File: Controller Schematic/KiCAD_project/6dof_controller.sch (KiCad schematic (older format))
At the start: 111 parts, among them J1 Screw_Terminal_01x03, J10 Conn_02x13_Top_Bottom, J2 DS-201, J3 RJ45, J4 Conn_02x13_Top_Bottom, J5 Conn_02x13_Top_Bottom, J6 Conn_02x13_Top_Bottom, J7 Conn_02x05_Top_Bottom, J8 Conn_02x13_Top_Bottom, J9 Conn_02x13_Top_Bottom, U1 4N35, U1 ESP32_DevKit_V1_DOIT, U10 4N35, U11 4N35, U12 4N35, U13 4N35, U14 4N35, U2 MCP23SigIn1M17_SP, U3 4N35, U4 4N35, U5 4N35, U6 4N35, U7 4N35, U8 4N35, U9 4N35

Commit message: I've renamed folders
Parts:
- J2: footprint Connector_BarrelJack:BarrelJack_Horizontal -> Connector_BarrelJack:BarrelJack_CUI_PJ-063AH_Horizontal
- renumbered *D11 to *D10, *D12 to *D11, *D3 to *D2, *D4 to *D3, *D5 to *D4, *D6 to *D5, *D7 to *D6, *D8 to *D7, *D9 to *D8, *D10 to *D9, *R2 to *R1, *R11 to *R10, *R12 to *R11, *R13 to *R12, *R14 to *R13, *R15 to *R14, *R16 to *R15, *R3 to *R2, *R4 to *R3, *R5 to *R4, *R6 to *R5, *R7 to *R6, *R8 to *R7, *R9 to *R8, *R10 to *R9, *U2 to *U1, *U3 to *U2, *U4 to *U3, *U5 to *U4, *U6 to *U5, *U7 to *U6, *U8 to *U7, *U9 to *U8, D2 to D1, D1 to D2, D2 to D3, D3 to D4, D4 to D5, D5 to D6, R9 to R10, R10 to R11, R11 to R12, R12 to R13, R13 to R14, R14 to R15, R1 to R2, R2 to R3, R3 to R4, R4 to R5, R5 to R6, R6 to R7, R7 to R8, R8 to R9, U9 to U10, U10 to U11, U11 to U12, U12 to U13, U13 to U14, U14 to U15, U1 to U2, U2 to U3, U3 to U4, U4 to U5, U5 to U6, U6 to U7, U7 to U8, U8 to U9

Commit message: project updated
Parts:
- removed J2: DS-201, Connector_BarrelJack:BarrelJack_CUI_PJ-063AH_Horizontal, symbol Connector:Barrel_Jack_Switch_Pin3Ring
- added J2: DS-201, Connector_BarrelJack:BarrelJack_CUI_PJ-063AH_Horizontal, symbol Connector:Barrel_Jack
- added JP4: SolderJumper_2_Open, Jumper:SolderJumper-2_P1.3mm_Open_Pad1.0x1.5mm, symbol Jumper:SolderJumper_2_Open
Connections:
- net COM: now also J2.2
- net NotSigOut1IN: now also JP4.2 (B)
- net at U3.27 (GPA6): now also JP4.1 (A)
- net at *J2.1 (Pin_1), D2.2 (A): now also J2.1
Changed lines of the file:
@@
 Wire Wire Line
 	1200 10650 1200 10250
-$Comp
-L Connector:Barrel_Jack_Switch_Pin3Ring J2
-U 1 1 601FD643
-P 900 10750
-F 0 "J2" H 950 11050 50  0000 C CNN
-F 1 "DS-201" H 957 10976 50  0000 C CNN
-F 2 "Connector_BarrelJack:BarrelJack_CUI_PJ-063AH_Horizontal" H 950 10710 50  0001 C CNN
-F 3 "https://www.chipdip.ru/product/ds-201" H 950 10710 50  0001 C CNN
-	1    900  10750
-	1    0    0    -1
-$EndComp
 Text GLabel 2500 10150 1    50   Input ~ 0
 DC12
@@
 Wire Wire Line
 	11200 4100 11300 4100
-Wire Wire Line
-	1200 10750 1200 10850
-Connection ~ 1200 10850
 Wire Bus Line
 	7500 650  7500 2050
@@
 	2550 10900 3050 10900
 Connection ~ 2550 10700
-$Comp
-L Jumper:SolderJumper_2_Open JP2
-U 1 1 602EB81E
-P 7100 2500
-F 0 "JP2" H 7250 2550 50  0000 C CNN
-F 1 "SolderJumper_2_Open" H 7100 2614 50  0001 C CNN
-F 2 "Jumper:SolderJumper-2_P1.3mm_Open_Pad1.0x1.5mm" H 7100 2500 50  0001 C CNN
-F 3 "~" H 7100 2500 50  0001 C CNN
-	1    7100 2500
-	1    0    0    -1
-$EndComp
-$Comp
-L Jumper:SolderJumper_2_Open JP3
-U 1 1 602ED0FE
-P 7100 2600
-F 0 "JP3" H 7100 2500 50  0000 C CNN
-F 1 "SolderJumper_2_Open" H 7100 2714 50  0001 C CNN
-F 2 "Jumper:SolderJumper-2_P1.3mm_Open_Pad1.0x1.5mm" H 7100 2600 50  0001 C CNN
-F 3 "~" H 7100 2600 50  0001 C CNN
-	1    7100 2600
-	1    0    0    -1
-$EndComp
 Text GLabel 7250 2500 2    50   Input ~ 0
 PanelLED
@@
 Wire Bus Line
 	7250 650  7250 5050
+$Comp
+L Jumper:SolderJumper_2_Open JP4
+U 1 1 5FCE05BC
+P 7100 2700
+F 0 "JP4" H 7250 2750 50  0000 C CNN
+F 1 "SolderJumper_2_Open" H 7100 2814 50  0001 C CNN
+F 2 "Jumper:SolderJumper-2_P1.3mm_Open_Pad1.0x1.5mm" H 7100 2700 50  0001 C CNN
+F 3 "~" H 7100 2700 50  0001 C CNN
+	1    7100 2700
+	1    0    0    -1
+$EndComp
+Text GLabel 7250 2700 2    50   Input ~ 0
+NotSigOut1IN
+$Comp
+L Jumper:SolderJumper_2_Open JP3
+U 1 1 602ED0FE
+P 7100 2600
+F 0 "JP3" H 7250 2650 50  0000 C CNN
+F 1 "SolderJumper_2_Open" H 7100 2714 50  0001 C CNN
+F 2 "Jumper:SolderJumper-2_P1.3mm_Open_Pad1.0x1.5mm" H 7100 2600 50  0001 C CNN
+F 3 "~" H 7100 2600 50  0001 C CNN
+	1    7100 2600
+	1    0    0    -1
+$EndComp
+$Comp
+L Jumper:SolderJumper_2_Open JP2
+U 1 1 602EB81E
+P 7100 2500
+F 0 "JP2" H 7250 2550 50  0000 C CNN
+F 1 "SolderJumper_2_Open" H 7100 2614 50  0001 C CNN
+F 2 "Jumper:SolderJumper-2_P1.3mm_Open_Pad1.0x1.5mm" H 7100 2500 50  0001 C CNN
+F 3 "~" H 7100 2500 50  0001 C CNN
+	1    7100 2500
+	1    0    0    -1
+$EndComp
+$Comp
+L Connector:Barrel_Jack J2
+U 1 1 5FCE9EE6
+P 900 10750
+F 0 "J2" H 957 11075 50  0000 C CNN
+F 1 "DS-201" H 957 10984 50  0000 C CNN
+F 2 "Connector_BarrelJack:BarrelJack_CUI_PJ-063AH_Horizontal" H 950 10710 50  0001 C CNN
+F 3 "https://www.chipdip.ru/product/ds-201" H 950 10710 50  0001 C CNN
+	1    900  10750
+	1    0    0    -1
+$EndComp
 $EndSCHEMATC

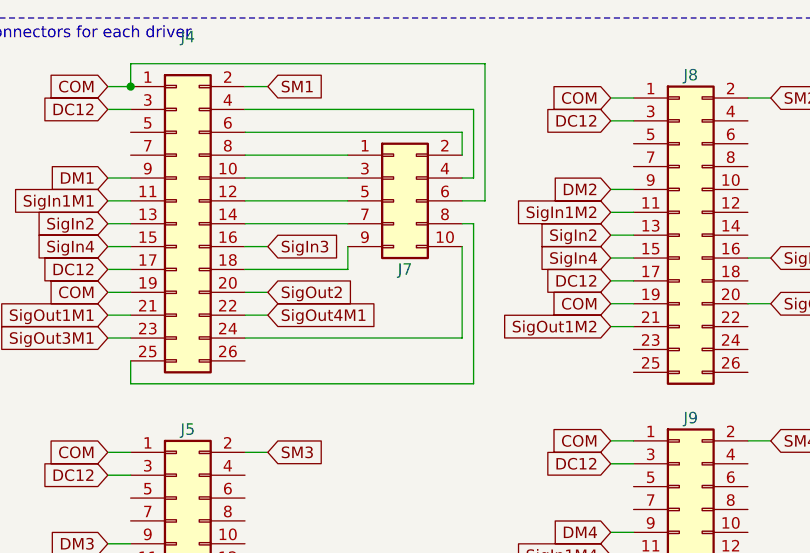
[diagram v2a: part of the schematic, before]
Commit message: I've added illustation for technical
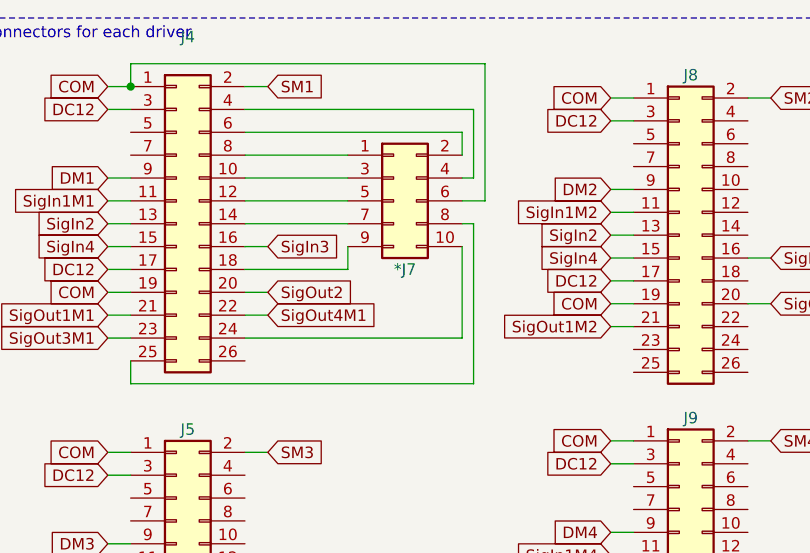
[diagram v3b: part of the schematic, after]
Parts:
- renumbered J7 to *J7
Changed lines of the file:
@@
 F 1 "1N4003" H 1500 10024 50  0000 C CNN
 F 2 "Diode_THT:D_DO-41_SOD81_P10.16mm_Horizontal" H 1500 9975 50  0001 C CNN
-F 3 "http://www.vishay.com/docs/88503/1n4001.pdf" H 1500 10150 50  0001 C CNN
+F 3 "https://www.chipdip.ru/product/1n4003-3" H 1500 10150 50  0001 C CNN
 	1    1500 10150
 	-1   0    0    1
@@
 F 1 "Conn_02x13_Top_Bottom" H 12750 3776 50  0001 C CNN
 F 2 "Connector_IDC:IDC-Header_2x13-1MP_P2.54mm_Latch_Vertical" H 12700 3050 50  0001 C CNN
-F 3 "~" H 12700 3050 50  0001 C CNN
+F 3 "https://www.chipdip.ru/product/idc-26ms" H 12700 3050 50  0001 C CNN
 	1    12700 3050
 	1    0    0    -1
@@
 F 1 "Conn_02x13_Top_Bottom" H 14950 5226 50  0001 C CNN
 F 2 "Connector_IDC:IDC-Header_2x13-1MP_P2.54mm_Latch_Vertical" H 14900 4500 50  0001 C CNN
-F 3 "~" H 14900 4500 50  0001 C CNN
+F 3 "https://www.chipdip.ru/product/idc-26ms" H 14900 4500 50  0001 C CNN
 	1    14900 4500
 	1    0    0    -1
@@
 F 1 "Conn_02x13_Top_Bottom" H 12750 5276 50  0001 C CNN
 F 2 "Connector_IDC:IDC-Header_2x13-1MP_P2.54mm_Latch_Vertical" H 12700 4550 50  0001 C CNN
-F 3 "~" H 12700 4550 50  0001 C CNN
+F 3 "https://www.chipdip.ru/product/idc-26ms" H 12700 4550 50  0001 C CNN
 	1    12700 4550
 	1    0    0    -1
@@
 F 1 "Conn_02x13_Top_Bottom" H 14950 3726 50  0001 C CNN
 F 2 "Connector_IDC:IDC-Header_2x13-1MP_P2.54mm_Latch_Vertical" H 14900 3000 50  0001 C CNN
-F 3 "~" H 14900 3000 50  0001 C CNN
+F 3 "https://www.chipdip.ru/product/idc-26ms" H 14900 3000 50  0001 C CNN
 	1    14900 3000
 	1    0    0    -1
@@
 F 1 "Conn_02x13_Top_Bottom" H 14950 2226 50  0001 C CNN
 F 2 "Connector_IDC:IDC-Header_2x13-1MP_P2.54mm_Latch_Vertical" H 14900 1500 50  0001 C CNN
-F 3 "~" H 14900 1500 50  0001 C CNN
+F 3 "https://www.chipdip.ru/product/idc-26ms" H 14900 1500 50  0001 C CNN
 	1    14900 1500
 	1    0    0    -1
@@
 	13450 1550 13450 1650
 $Comp
-L Connector_Generic:Conn_02x05_Odd_Even J7
+L Connector_Generic:Conn_02x05_Odd_Even *J7
 U 1 1 608ED766
 P 13650 1350
-F 0 "J7" H 13700 1050 50  0000 C CNN
+F 0 "*J7" H 13700 1050 50  0000 C CNN
 F 1 "Conn_02x05_Top_Bottom" H 13700 1676 50  0001 C CNN
 F 2 "Connector_IDC:IDC-Header_2x05_P2.54mm_Vertical" H 13650 1350 50  0001 C CNN
@@
 F 1 "Conn_02x13_Top_Bottom" H 12750 2176 50  0001 C CNN
 F 2 "Connector_IDC:IDC-Header_2x13-1MP_P2.54mm_Latch_Vertical" H 12700 1450 50  0001 C CNN
-F 3 "~" H 12700 1450 50  0001 C CNN
+F 3 "https://www.chipdip.ru/product/idc-26ms" H 12700 1450 50  0001 C CNN
 	1    12700 1450
 	1    0    0    -1
@@
 Text GLabel 7250 2600 2    50   Input ~ 0
 PanelIN
+$Comp
+L Jumper:SolderJumper_2_Open JP4
+U 1 1 5FCE05BC
+P 7100 2700
+F 0 "JP4" H 7250 2750 50  0000 C CNN
+F 1 "SolderJumper_2_Open" H 7100 2814 50  0001 C CNN
+F 2 "Jumper:SolderJumper-2_P1.3mm_Open_Pad1.0x1.5mm" H 7100 2700 50  0001 C CNN
+F 3 "~" H 7100 2700 50  0001 C CNN
+	1    7100 2700
+	1    0    0    -1
+$EndComp
+Text GLabel 7250 2700 2    50   Input ~ 0
+NotSigOut1IN
+$Comp
+L Jumper:SolderJumper_2_Open JP3
+U 1 1 602ED0FE
+P 7100 2600
+F 0 "JP3" H 7250 2650 50  0000 C CNN
+F 1 "SolderJumper_2_Open" H 7100 2714 50  0001 C CNN
+F 2 "Jumper:SolderJumper-2_P1.3mm_Open_Pad1.0x1.5mm" H 7100 2600 50  0001 C CNN
+F 3 "~" H 7100 2600 50  0001 C CNN
+	1    7100 2600
+	1    0    0    -1
+$EndComp
+$Comp
+L Jumper:SolderJumper_2_Open JP2
+U 1 1 602EB81E
+P 7100 2500
+F 0 "JP2" H 7250 2550 50  0000 C CNN
+F 1 "SolderJumper_2_Open" H 7100 2614 50  0001 C CNN
+F 2 "Jumper:SolderJumper-2_P1.3mm_Open_Pad1.0x1.5mm" H 7100 2500 50  0001 C CNN
+F 3 "~" H 7100 2500 50  0001 C CNN
+	1    7100 2500
+	1    0    0    -1
+$EndComp
+$Comp
+L Connector:Barrel_Jack J2
+U 1 1 5FCE9EE6
+P 900 10750
+F 0 "J2" H 957 11075 50  0000 C CNN
+F 1 "DS-201" H 957 10984 50  0000 C CNN
+F 2 "Connector_BarrelJack:BarrelJack_CUI_PJ-063AH_Horizontal" H 950 10710 50  0001 C CNN
+F 3 "https://www.chipdip.ru/product/ds-201" H 950 10710 50  0001 C CNN
+	1    900  10750
+	1    0    0    -1
+$EndComp
 Wire Bus Line
 	7800 1100 7800 2050
@@
 Wire Bus Line
 	7250 650  7250 5050
-$Comp
-L Jumper:SolderJumper_2_Open JP4
-U 1 1 5FCE05BC
-P 7100 2700
-F 0 "JP4" H 7250 2750 50  0000 C CNN
-F 1 "SolderJumper_2_Open" H 7100 2814 50  0001 C CNN
-F 2 "Jumper:SolderJumper-2_P1.3mm_Open_Pad1.0x1.5mm" H 7100 2700 50  0001 C CNN
-F 3 "~" H 7100 2700 50  0001 C CNN
-	1    7100 2700
-	1    0    0    -1
-$EndComp
-Text GLabel 7250 2700 2    50   Input ~ 0
-NotSigOut1IN
-$Comp
-L Jumper:SolderJumper_2_Open JP3
-U 1 1 602ED0FE
-P 7100 2600
-F 0 "JP3" H 7250 2650 50  0000 C CNN
-F 1 "SolderJumper_2_Open" H 7100 2714 50  0001 C CNN
-F 2 "Jumper:SolderJumper-2_P1.3mm_Open_Pad1.0x1.5mm" H 7100 2600 50  0001 C CNN
-F 3 "~" H 7100 2600 50  0001 C CNN
-	1    7100 2600
-	1    0    0    -1
-$EndComp
-$Comp
-L Jumper:SolderJumper_2_Open JP2
-U 1 1 602EB81E
-P 7100 2500
-F 0 "JP2" H 7250 2550 50  0000 C CNN
-F 1 "SolderJumper_2_Open" H 7100 2614 50  0001 C CNN
-F 2 "Jumper:SolderJumper-2_P1.3mm_Open_Pad1.0x1.5mm" H 7100 2500 50  0001 C CNN
-F 3 "~" H 7100 2500 50  0001 C CNN
-	1    7100 2500
-	1    0    0    -1
-$EndComp
-$Comp
-L Connector:Barrel_Jack J2
-U 1 1 5FCE9EE6
-P 900 10750
-F 0 "J2" H 957 11075 50  0000 C CNN
-F 1 "DS-201" H 957 10984 50  0000 C CNN
-F 2 "Connector_BarrelJack:BarrelJack_CUI_PJ-063AH_Horizontal" H 950 10710 50  0001 C CNN
-F 3 "https://www.chipdip.ru/product/ds-201" H 950 10710 50  0001 C CNN
-	1    900  10750
-	1    0    0    -1
-$EndComp
 $EndSCHEMATC

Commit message: The circuit and board were redesigned after prototyping. Removed all unnecessary. Reduced the PCB.
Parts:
- removed *D10, *D3, *D8, *D9, D1: BL-LS0805UYC, LED_SMD:LED_0805_2012Metric, symbol Device:LED
- removed *D5, *D6, *D7: BAV23, Package_TO_SOT_SMD:SOT-23, symbol Diode:BAV70
- removed *J1: Screw_Terminal_01x02, TerminalBlock_Phoenix:TerminalBlock_Phoenix_MKDS-1,5-2_1x02_P5.00mm_Horizontal, symbol Connector:Screw_Terminal_01x02
- removed *R10, *R14, *R3, *R4, *R5, *R6, *R7, *R8, *R9, R1: 330, Resistor_SMD:R_0805_2012Metric, symbol Device:R
- removed *R11, *R12, *R13, *R2: 100, Resistor_SMD:R_0805_2012Metric, symbol Device:R
- removed *U1, *U4, *U5, *U6, *U7, U2: 4N35, Package_DIP:SMDIP-6_W9.53mm, symbol Isolator:4N35
- removed *U3: MCP23SigIn1M17_SP, Package_DIP:DIP-28_W7.62mm, symbol Interface_Expansion:MCP23S17_SP
- removed DS1: WC1602A, Display:WC1602A, symbol Display_Character:WC1602A
- removed JP1: SolderJumper_2_Bridged, Jumper:SolderJumper-2_P1.3mm_Bridged_RoundedPad1.0x1.5mm, symbol Jumper:SolderJumper_2_Bridged
- removed RV1: R_POT, Potentiometer_THT:Potentiometer_Bourns_3339W_Horizontal, symbol Device:R_POT
- added JP1, JP10, JP11, JP12, JP13, JP14, JP5, JP6, JP7, JP8, JP9: SolderJumper_2_Open, Jumper:SolderJumper-2_P1.3mm_Open_RoundedPad1.0x1.5mm, symbol Jumper:SolderJumper_2_Open
- JP2, JP3, JP4: footprint Jumper:SolderJumper-2_P1.3mm_Open_Pad1.0x1.5mm -> Jumper:SolderJumper-2_P1.3mm_Open_RoundedPad1.0x1.5mm
- renumbered *D4 to *D3, *D11 to *D4, *J2 to *J1, *J3 to *J2, *J7 to *J3, *R15 to *R2, *U2 to *U1, *U8 to *U2, D2 to D1, D3 to D2, D4 to D3, D5 to D4, D6 to D5, J8 to J7, J9 to J8, J10 to J9, R2 to R1, R11 to R10, R12 to R11, R13 to R12, R14 to R13, R15 to R14, R3 to R2, R4 to R3, R5 to R4, R6 to R5, R7 to R6, R8 to R7, R9 to R8, R10 to R9, U11 to U10, U12 to U11, U13 to U12, U14 to U13, U15 to U14, U3 to U2, U4 to U3, U5 to U4, U6 to U5, U7 to U6, U8 to U7, U9 to U8, U10 to U9
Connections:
- net NotSigOut1IN is gone; now on net DirM5: JP4.2 (B)
- net PanelIN is gone; now on net StepM5: JP3.2 (B)
- net PanelLED is gone; now on net DirM4: JP2.2 (B)
- net BTN1IN: now also U1.29 (IO22), JP8.2 (B); no longer U2.28 (GPA7)
- net DC12: now also J1.3 (Pin_3)
- net DirM1: now also JP10.2 (B); no longer *XA1.10 (A1)
- net DirM2: now also JP12.2 (B); no longer *XA1.12 (A3)
- net DirM3: now also JP14.2 (B); no longer *XA1.14 (SCL/A5)
- net DirM6: now also JP6.2 (B)
- net SigOut2: now also *D4.1 (K)
- net SigOut2IN: now also U1.30 (IO23), JP7.2 (B); no longer *D4.1 (K)
- net StepM1: now also JP9.2 (B); no longer *XA1.9 (A0)
- net StepM2: now also JP11.2 (B); no longer *XA1.11 (A2)
- net StepM3: now also JP13.2 (B); no longer *XA1.13 (SDA/A4)
- net StepM4: now also JP1.2 (B)
- net StepM6: now also JP5.2 (B)
- net at JP4.1 (A): now also *XA1.20 (D5); no longer U2.27 (GPA6)
- net at *R2.2, *U2.1: now also *D4.2 (A)
- net at *XA1.23 (D8): now also JP7.1 (A)
- net at JP2.1 (A): now also *XA1.18 (D3); no longer U2.25 (GPA4)
- net at JP3.1 (A): now also *XA1.19 (D4); no longer U2.26 (GPA5)
- net at J1.2 (Pin_2): now also *D1.2 (A), *R1.1, *U1.1
- net CSigIn1M1: no longer names the net of U1.21 (IO16)
- net CSigIn1M1: no longer *XA1.24 (D9)
- net LCDD2: no longer names the net of *XA1.17 (D2)
- net LCDD2: now also JP1.1 (A); no longer U1.29 (IO22)
- net LCDD3: no longer names the net of U1.26 (IO21)
- net LCDD3: no longer *XA1.18 (D3)
- net LCDD4: no longer names the net of U1.5 (IO35)
- net LCDD4: no longer *XA1.19 (D4)
- net LCDD5: no longer names the net of U1.24 (IO18)
- net LCDD5: no longer *XA1.20 (D5)
- net LCDD6: no longer names the net of *XA1.21 (D6)
- net LCDD6: now also JP5.1 (A); no longer U1.30 (IO23)
- net LCDD7: no longer names the net of U1.25 (IO19)
- net LCDD7: no longer *XA1.22 (D7)
- new net: *XA1.10 (A1), JP10.1 (A)
- new net: *XA1.11 (A2), JP11.1 (A)
- new net: *XA1.12 (A3), JP12.1 (A)
- new net: *XA1.13 (SDA/A4), JP13.1 (A)
- new net: *XA1.14 (SCL/A5), JP14.1 (A)
- new net: *XA1.22 (D7), JP6.1 (A)
- new net: *XA1.24 (D9), JP8.1 (A)
- new net: *XA1.9 (A0), JP9.1 (A)
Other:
- note removed: "Digital outputs"
- note removed: "I/O Expanders #2"
- note removed: "LCD Display"
- note removed: "SigOut1 signals from drivers"
- note removed: "platform activation toggle switch"
- moved on the sheet: *D1, *D2, *D3, *D4, *J1, *J2, *R1, *R2, *U1, *XA1, C1, C10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

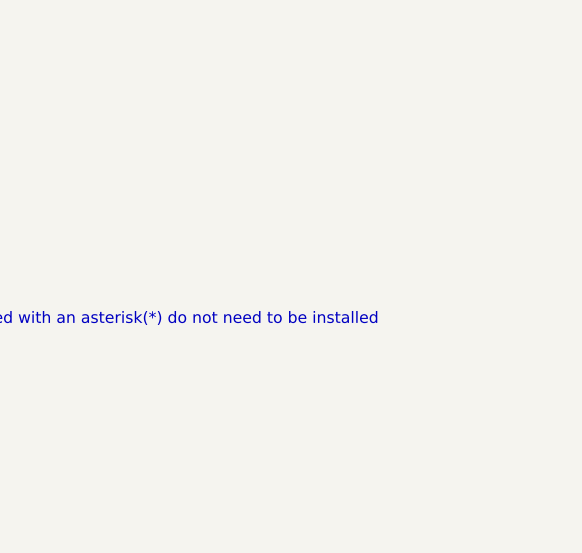
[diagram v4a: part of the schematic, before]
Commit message: Added PCB image
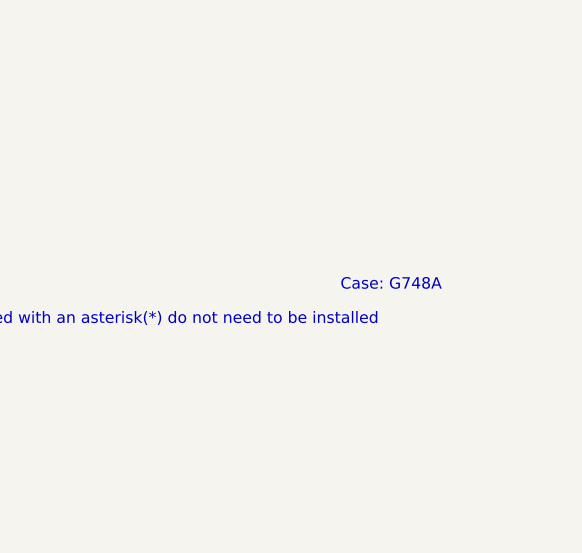
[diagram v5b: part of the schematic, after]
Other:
- note added: "Case: G748A"
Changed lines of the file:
@@
 Wire Bus Line
 	7250 650  7250 3400
+Text Notes 15500 9750 0    50   ~ 0
+Case: G748A
 $EndSCHEMATC

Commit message: I've modified schematic and PCB for 6DOF controller
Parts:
- added LOGO1: Logo_Open_Hardware_Large, Symbol:OSHW-Logo2_14.6x12mm_Copper, symbol Graphic:Logo_Open_Hardware_Large
- *D1, *D4, D2, D3, D4, D5: footprint LED_SMD:LED_0805_2012Metric -> LED_SMD:LED_0805_2012Metric_Pad1.15x1.40mm_HandSolder
- R1: value 330 -> 1K
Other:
- note added: "D4, D5 NOT INSTALL (for future use)"
- note added: "NOT INSTALL (for future use)"
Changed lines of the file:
@@
 F 0 "D3" V 13400 7850 50  0000 R CNN
 F 1 "BL-LS0805UYC" V 13348 7532 50  0001 R CNN
-F 2 "LED_SMD:LED_0805_2012Metric" H 13400 7650 50  0001 C CNN
+F 2 "LED_SMD:LED_0805_2012Metric_Pad1.15x1.40mm_HandSolder" H 13400 7650 50  0001 C CNN
 F 3 "https://www.chipdip.ru/product/bl-ls0805uyc" H 13400 7650 50  0001 C CNN
 F 4 "https://www.chipdip.ru/product/bl-ls0805uyc" V 13400 7650 50  0001 C CNN "Field4"
@@
 F 0 "*D1" V 7500 7700 50  0000 R CNN
 F 1 "BL-LS0805UYC" V 7548 7432 50  0001 R CNN
-F 2 "LED_SMD:LED_0805_2012Metric" H 7600 7550 50  0001 C CNN
+F 2 "LED_SMD:LED_0805_2012Metric_Pad1.15x1.40mm_HandSolder" H 7600 7550 50  0001 C CNN
 F 3 "https://www.chipdip.ru/product/bl-ls0805uyc" H 7600 7550 50  0001 C CNN
 F 4 "https://www.chipdip.ru/product/bl-ls0805uyc" V 7600 7550 50  0001 C CNN "Field4"
@@
 F 0 "D2" V 10500 7750 50  0000 R CNN
 F 1 "BL-LS0805UYC" V 10448 7682 50  0001 R CNN
-F 2 "LED_SMD:LED_0805_2012Metric" H 10500 7800 50  0001 C CNN
+F 2 "LED_SMD:LED_0805_2012Metric_Pad1.15x1.40mm_HandSolder" H 10500 7800 50  0001 C CNN
 F 3 "https://www.chipdip.ru/product/bl-ls0805uyc" H 10500 7800 50  0001 C CNN
 F 4 "https://www.chipdip.ru/product/bl-ls0805uyc" V 10500 7800 50  0001 C CNN "Field4"
@@
 P 10500 7450
 F 0 "R1" H 10570 7496 50  0000 L CNN
-F 1 "330" H 10570 7405 50  0000 L CNN
+F 1 "1K" H 10570 7405 50  0000 L CNN
 F 2 "Resistor_SMD:R_0805_2012Metric" V 10430 7450 50  0001 C CNN
 F 3 "https://www.chipdip.ru/product0/9000079474" H 10500 7450 50  0001 C CNN
@@
 F 0 "D5" V 10339 1032 50  0000 R CNN
 F 1 "BL-LS0805UYC" V 10248 1032 50  0001 R CNN
-F 2 "LED_SMD:LED_0805_2012Metric" H 10300 1150 50  0001 C CNN
+F 2 "LED_SMD:LED_0805_2012Metric_Pad1.15x1.40mm_HandSolder" H 10300 1150 50  0001 C CNN
 F 3 "https://www.chipdip.ru/product/bl-ls0805uyc" H 10300 1150 50  0001 C CNN
 F 4 "https://www.chipdip.ru/product/bl-ls0805uyc" V 10300 1150 50  0001 C CNN "Field4"
@@
 F 0 "D4" V 8489 1032 50  0000 R CNN
 F 1 "BL-LS0805UYC" V 8398 1032 50  0001 R CNN
-F 2 "LED_SMD:LED_0805_2012Metric" H 8450 1150 50  0001 C CNN
+F 2 "LED_SMD:LED_0805_2012Metric_Pad1.15x1.40mm_HandSolder" H 8450 1150 50  0001 C CNN
 F 3 "https://www.chipdip.ru/product/bl-ls0805uyc" H 8450 1150 50  0001 C CNN
 F 4 "https://www.chipdip.ru/product/bl-ls0805uyc" V 8450 1150 50  0001 C CNN "Field4"
@@
 F 0 "*D4" V 13350 6200 50  0000 R CNN
 F 1 "BL-LS0805UYC" V 13298 6132 50  0001 R CNN
-F 2 "LED_SMD:LED_0805_2012Metric" H 13350 6250 50  0001 C CNN
+F 2 "LED_SMD:LED_0805_2012Metric_Pad1.15x1.40mm_HandSolder" H 13350 6250 50  0001 C CNN
 F 3 "https://www.chipdip.ru/product/bl-ls0805uyc" H 13350 6250 50  0001 C CNN
 F 4 "https://www.chipdip.ru/product/bl-ls0805uyc" V 13350 6250 50  0001 C CNN "Field4"
@@
 Wire Notes Line
 	11600 5200 10200 5200
+Text Notes 15500 9750 0    50   ~ 0
+Case: G748A
 Wire Bus Line
 	7800 1100 7800 2050
@@
 Wire Bus Line
 	7250 650  7250 3400
-Text Notes 15500 9750 0    50   ~ 0
-Case: G748A
+Text Notes 11850 6750 0    50   ~ 0
+NOT INSTALL (for future use)
+Text Notes 7950 7950 0    50   ~ 0
+NOT INSTALL (for future use)
+Text Notes 7750 4800 0    50   ~ 0
+D4, D5 NOT INSTALL (for future use)
+$Comp
+L Graphic:Logo_Open_Hardware_Large LOGO1
+U 1 1 60181939
+P 9750 10500
+F 0 "LOGO1" H 9750 11000 50  0001 C CNN
+F 1 "Logo_Open_Hardware_Large" H 9750 10100 50  0001 C CNN
+F 2 "Symbol:OSHW-Logo2_14.6x12mm_Copper" H 10216 10550 50  0000 L CNN
+F 3 "~" H 9750 10500 50  0001 C CNN
+	1    9750 10500
+	1    0    0    -1
+$EndComp
 $EndSCHEMATC
